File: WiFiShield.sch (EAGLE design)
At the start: 38 parts, among them IC1 74HC4050D, IC2 SPX3819M5-L-3-3, IC3 CC3000MOD, IC4 MCP9701A, J1 Test, J10 U.FL-R-SMT-1(10), J11 Mode, J12 Temp, J5 ARDUINO-SHIELD_R3, J6 101-00660-68-6

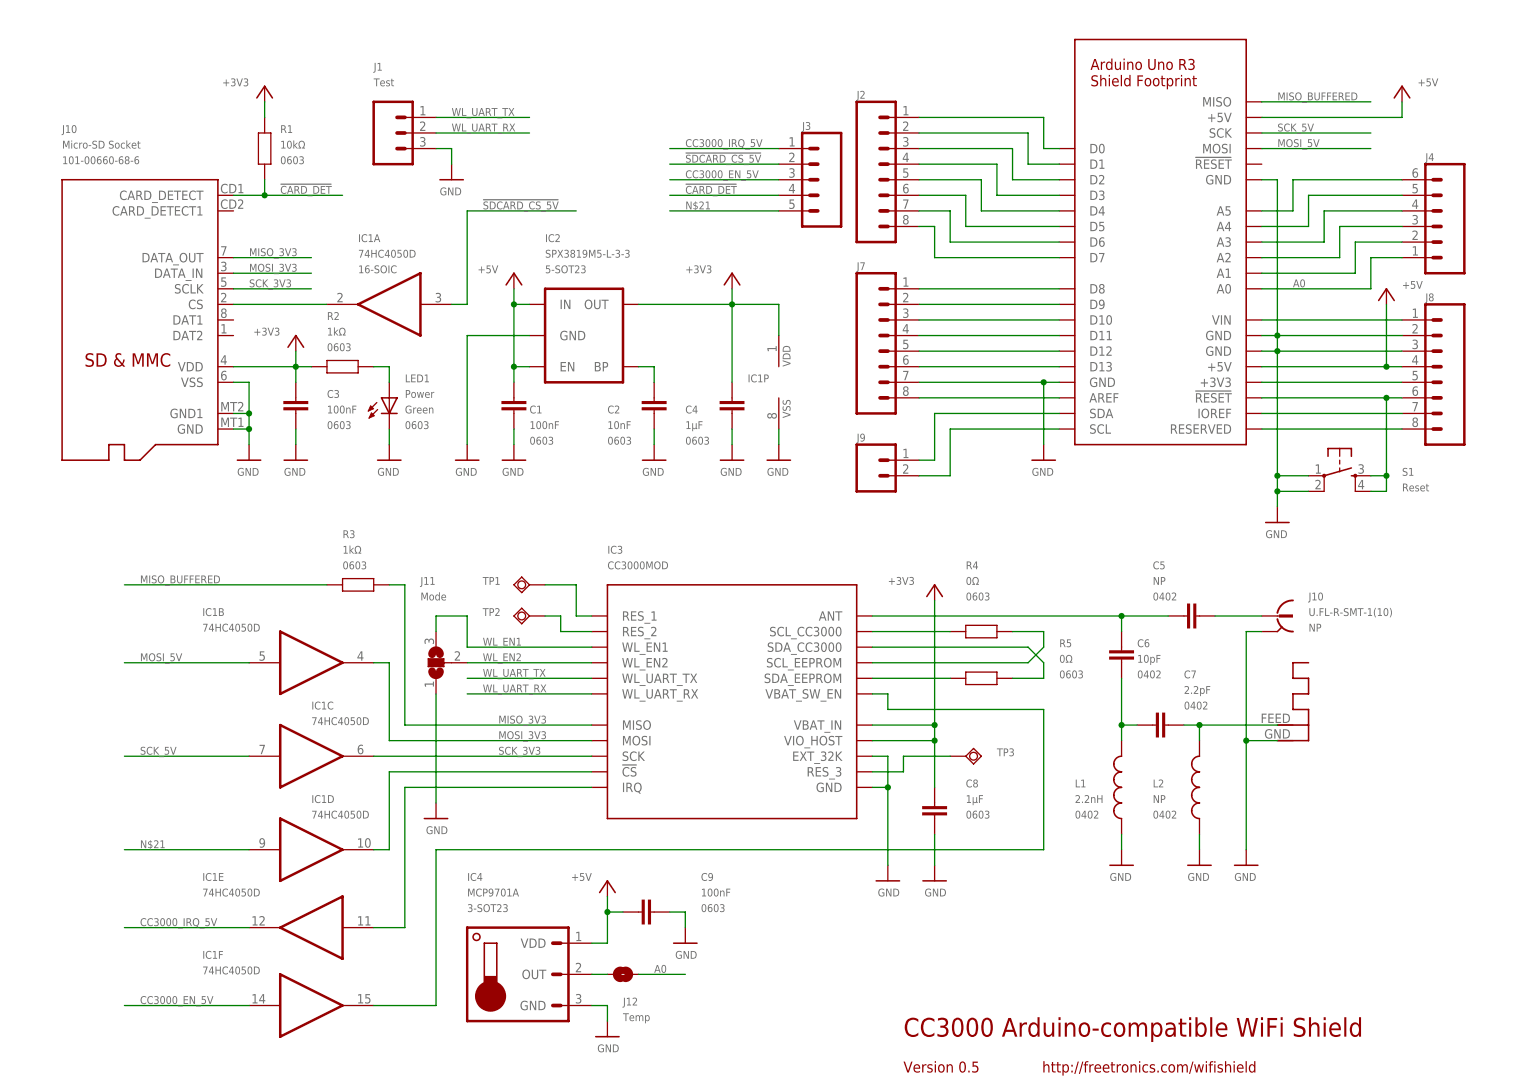
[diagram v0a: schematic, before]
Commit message: Added tristate buffer on MISO to fix CC3000 SPI bug, some minor tweaks, pull-ups added on nCS lines and CC3000 enable, silkscreen label tweaks.
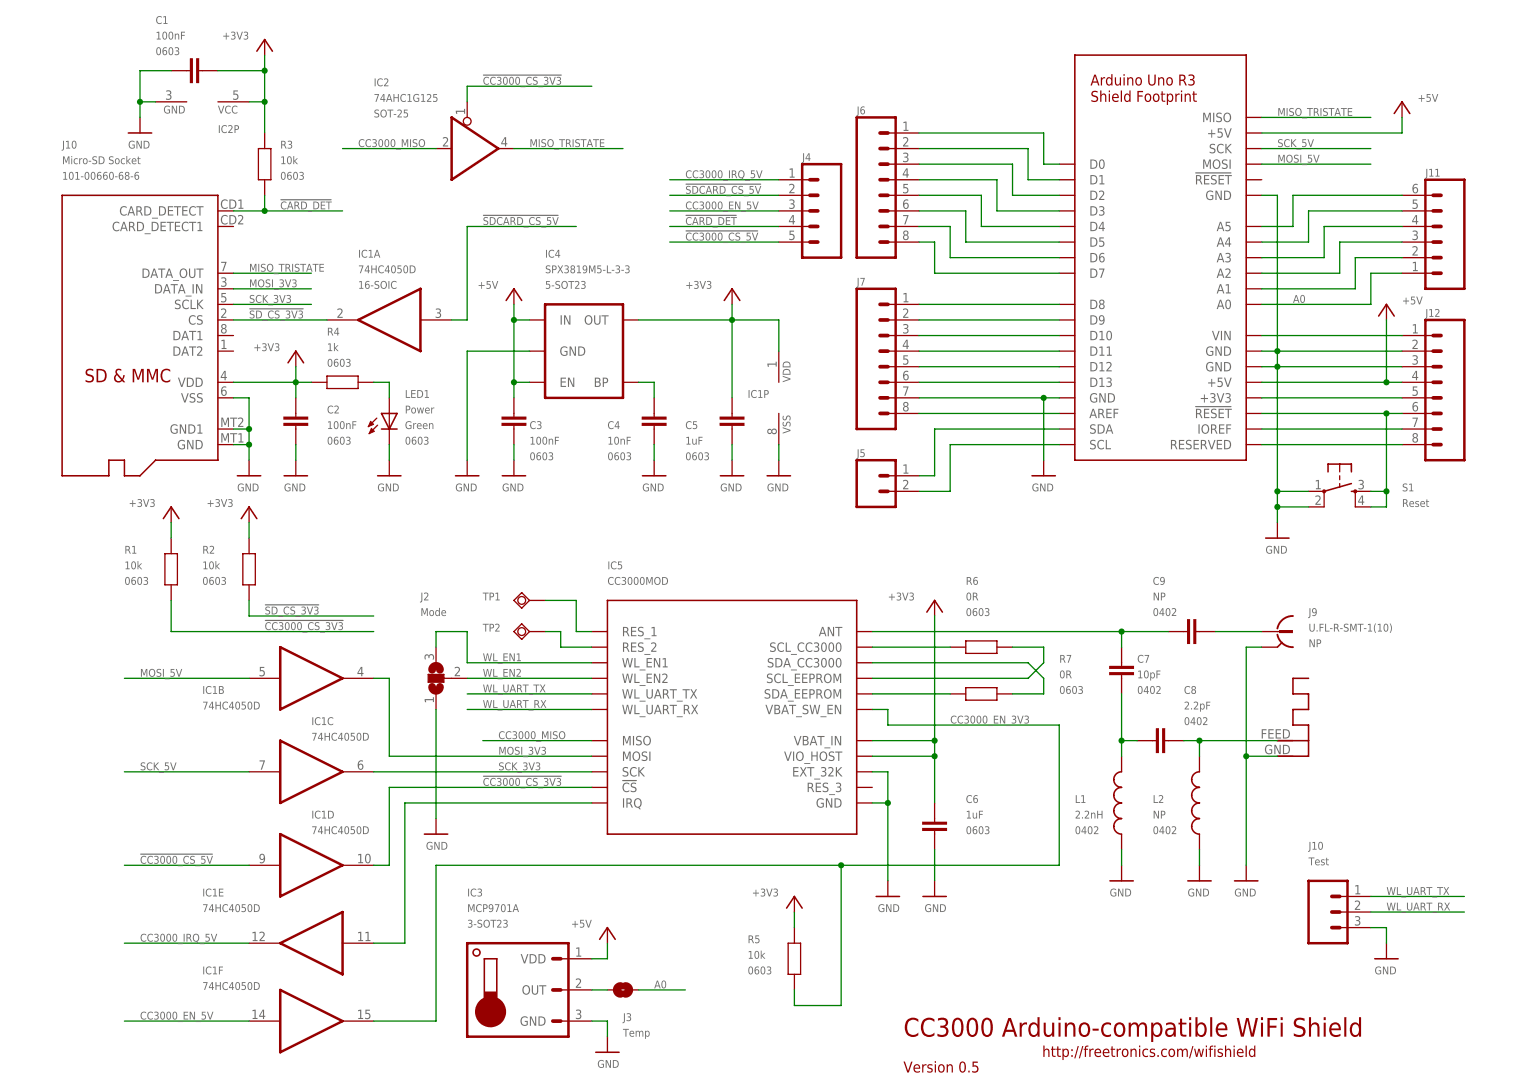
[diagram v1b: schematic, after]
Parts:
- removed TP3: R3, testpad:TPSQTP06R
- added IC5: CC3000MOD, freetronics-luke:CC3000
- added R6, R7: 0R, freetronics-master-v1:RESISTOR0603
- C2: value 10nF -> 100nF
- C4: value 1µF -> 10nF
- C5: value NP -> 1uF; device freetronics-master-v1:CAP0402 -> freetronics-master-v1:CAP0603; PACKAGE 0402 -> 0603
- C6: value 10pF -> 1uF; device freetronics-master-v1:CAP0402 -> freetronics-master-v1:CAP0603; PACKAGE 0402 -> 0603
- C7: value 2.2pF -> 10pF
- C8: value 1µF -> 2.2pF; device freetronics-master-v1:CAP0603 -> freetronics-master-v1:CAP0402; PACKAGE 0603 -> 0402
- C9: value 100nF -> NP; device freetronics-master-v1:CAP0603 -> freetronics-master-v1:CAP0402; PACKAGE 0603 -> 0402
- IC2: value SPX3819M5-L-3-3 -> 74AHC1G125; device SparkFun:V_REG_LDOSMD -> 74xx-little-de:74AHC1G125DBV; PACKAGE 5-SOT23 -> SOT-25
- IC3: value CC3000MOD -> MCP9701A; device freetronics-luke:CC3000 -> freetronics-master-v1:MCP9700SOT-23; PACKAGE (none) -> 3-SOT23
- IC4: value MCP9701A -> SPX3819M5-L-3-3; device freetronics-master-v1:MCP9700SOT-23 -> SparkFun:V_REG_LDOSMD; PACKAGE 3-SOT23 -> 5-SOT23
- J1: value Test -> 101-00660-68-6; device freetronics-master-v1:M03PTH -> RAMPSdisplay:ADAFRUIT_MICROSD; FOO (none) -> Micro-SD Socket; ID (none) -> 101-00660-68-6; NAME2 (none) -> J10
- J10: value U.FL-R-SMT-1(10) -> Test; device freetronics-luke:UFL -> freetronics-master-v1:M03PTH; NOTE NP -> (none)
- J11: value Mode -> (none); device freetronics-master-v1:SJ2W -> freetronics-master-v1:M06SIP
- J12: value Temp -> (none); device freetronics-luke:SJ -> freetronics-master-v1:M08STD
- J2: value (none) -> Mode; device freetronics-master-v1:M08STD -> freetronics-master-v1:SJ2W
- J3: value (none) -> Temp; device freetronics-master-v1:M05PTH -> freetronics-luke:SJ
- J4: device freetronics-master-v1:M06SIP -> freetronics-master-v1:M05PTH
- J5: value ARDUINO-SHIELD_R3 -> (none); device freetronics-luke:ARDUINO-SHIELD_R3 -> freetronics-master-v1:M02PTH
- J6: value 101-00660-68-6 -> (none); device RAMPSdisplay:ADAFRUIT_MICROSD -> freetronics-master-v1:M08STD; FOO Micro-SD Socket -> (none); ID 101-00660-68-6 -> (none); NAME2 J10 -> (none)
- J8: value (none) -> ARDUINO-SHIELD_R3; device freetronics-master-v1:M08STD -> freetronics-luke:ARDUINO-SHIELD_R3
- J9: value (none) -> U.FL-R-SMT-1(10); device freetronics-master-v1:M02PTH -> freetronics-luke:UFL; NOTE (none) -> NP
- R1: value 10kΩ -> 10k
- R2, R3: value 1kΩ -> 10k
- R4: value 0Ω -> 1k
- R5: value 0Ω -> 10k
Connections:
- removed net MISO_3V3: IC3.MISO, J6.DATA_OUT, R3.1
- removed net MISO_BUFFERED: J5.MISO, R3.2
- removed net N$21: IC1D.I, J3.5
- removed net N$3: IC1F.O, IC3.VBAT_SW_EN
- removed net N$35: IC1A.O, J6.CS
- removed net N$41: IC1D.O, IC3.!CS
- removed net RES_3: IC3.RES_3, TP3.TP
- new net !CC3000_CS_3V3: IC1D.O, IC2A.OE, IC5.!CS, R1.2
- new net !CC3000_CS_5V: IC1D.I, J4.5
- new net !SD_CS_3V3: IC1A.O, J1.CS, R2.2
- new net CC3000_EN_3V3: IC1F.O, IC5.VBAT_SW_EN, R5.2
- new net CC3000_MISO: IC2A.I, IC5.MISO
- new net MISO_TRISTATE: IC2A.O, J1.DATA_OUT, J8.MISO
- net !CARD_DET: now also J1.CARD_DETECT, J4.4, R3.1; no longer J3.4, J6.CARD_DETECT, R1.1
- net !SDCARD_CS_5V: now also J4.2; no longer J3.2
- net +3V3: now also C1.2, C2.1, C5.1, C6.2, IC2P.VCC, IC4.OUT, IC5.VBAT_IN, IC5.VIO_HOST, J1.VDD, R1.1, R2.1, R3.2, R4.2, R5.1; no longer C3.1, C4.1, C8.2, IC2.OUT, IC3.VBAT_IN, IC3.VIO_HOST, J6.VDD, R1.2, R2.2
- net +5V: now also C3.2, IC4.EN, IC4.IN, J12.4, J8.+5V; no longer C1.2, IC2.EN, IC2.IN, J5.+5V, J8.4
- net +5V-2: now also IC3.VDD, J8.+5V@0; no longer C9.1, IC4.VDD, J5.+5V@0
- net A0: now also J11.1, J3.2, J8.A0; no longer J12.2, J4.1, J5.A0
- net CC3000_EN_5V: now also J4.3; no longer J3.3
- net CC3000_IRQ_5V: now also J4.1; no longer J3.1
- net GND: now also C2.2, C3.1, C4.1, C5.2, C6.1, IC2P.GND, IC5.EXT_32K, IC5.GND, J1.GND, J1.GND1, J1.VSS, J10.3, J12.2, J12.3, J2.1, J8.GND, J8.GND@0, J8.GND@1, J8.GND@2, J9.GND; no longer C2.1, C3.2, C4.2, C8.1, C9.2, IC2.GND, IC3.EXT_32K, J1.3, J10.GND, J11.1, J5.GND, J5.GND@0, J5.GND@1, J5.GND@2, J6.GND, J6.GND1, J6.VSS, J8.2, J8.3
- net MOSI_3V3: now also IC5.MOSI, J1.DATA_IN; no longer IC3.MOSI, J6.DATA_IN
- net MOSI_5V: now also J8.MOSI; no longer J5.MOSI
- net N$1: now also IC5.SDA_EEPROM, R7.2; no longer IC3.SDA_EEPROM, R5.2
- net N$103: now also C7.1, C8.2; no longer C6.1, C7.2
- net N$104: now also C8.1; no longer C7.1
- net N$11: now also IC3.OUT, J3.1; no longer IC4.OUT, J12.1
- net N$123: now also J6.6, J8.D5; no longer J2.6, J5.D5
- net N$124: now also J6.7, J8.D6; no longer J2.7, J5.D6
- net N$125: now also J6.8, J8.D7; no longer J2.8, J5.D7
- net N$126: now also J5.1, J8.SDA; no longer J5.SDA, J9.1
- net N$127: now also J8.AREF; no longer J5.AREF
- net N$128: now also J8.D13; no longer J5.D13
- net N$129: now also J8.D12; no longer J5.D12
- net N$130: now also J5.2, J8.SCL; no longer J5.SCL, J9.2
- net N$131: now also J8.D8; no longer J5.D8
- net N$132: now also J8.D9; no longer J5.D9
- net N$133: now also J8.D10; no longer J5.D10
- net N$134: now also J8.D11; no longer J5.D11
- net N$15: now also IC5.SCL_CC3000, R6.2; no longer IC3.SCL_CC3000, R4.2
- net N$16: now also C7.2, C9.2, IC5.ANT; no longer C5.2, C6.2, IC3.ANT
- net N$2: now also IC5.SDA_CC3000, R7.1; no longer IC3.SDA_CC3000, R5.1
- net N$28: now also IC5.RES_2; no longer IC3.RES_2
- net N$29: now also IC5.RES_1; no longer IC3.RES_1
- net N$30: now also C9.1, J9.SIG; no longer C5.1, J10.SIG
- net N$4: now also R4.1; no longer R2.1
- net N$42: now also IC5.IRQ; no longer IC3.IRQ
- net N$43: now also C4.2, IC4.BP; no longer C2.2, IC2.BP
- net N$48: now also J11.2, J8.A1; no longer J4.2, J5.A1
- net N$49: now also J11.3, J8.A2; no longer J4.3, J5.A2
- net N$5: now also IC5.SCL_EEPROM, R6.1; no longer IC3.SCL_EEPROM, R4.1
- net N$50: now also J11.4, J8.A3; no longer J4.4, J5.A3
- net N$72: now also J11.5, J8.A4; no longer J4.5, J5.A4
- net N$73: now also J11.6, J8.A5; no longer J4.6, J5.A5
- net N$74: now also J12.8, J8.RESERVED; no longer J5.RESERVED, J8.8
- net N$75: now also J12.1, J8.VIN; no longer J5.VIN, J8.1
- net N$77: now also J12.5, J8.+3V3; no longer J5.+3V3, J8.5
- net N$78: now also J12.6, J8.!RESET; no longer J5.!RESET, J8.6
- net N$81: now also J12.7, J8.IOREF; no longer J5.IOREF, J8.7
- net N$82: now also J6.1, J8.D0; no longer J2.1, J5.D0
- net N$87: now also J6.2, J8.D1; no longer J2.2, J5.D1
- net N$88: now also J6.3, J8.D2; no longer J2.3, J5.D2
- net N$89: now also J6.4, J8.D3; no longer J2.4, J5.D3
- net N$90: now also J6.5, J8.D4; no longer J2.5, J5.D4
- net SCK_3V3: now also IC5.SCK, J1.SCLK; no longer IC3.SCK, J6.SCLK
- net SCK_5V: now also J8.SCK; no longer J5.SCK
- net WL_EN1: now also IC5.WL_EN1, J2.3; no longer IC3.WL_EN1, J11.3
- net WL_EN2: now also IC5.WL_EN2, J2.2; no longer IC3.WL_EN2, J11.2
- net WL_UART_RX: now also IC5.WL_UART_RX, J10.2; no longer IC3.WL_UART_RX, J1.2
- net WL_UART_TX: now also IC5.WL_UART_TX, J10.1; no longer IC3.WL_UART_TX, J1.1
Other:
- note removed: "PCB Stackup: 2-layer FR-4, must be 0.8 mm thick 35µm Cu both layers, with mask"
- moved on the sheet: C1, C2, C3, C4, C5, C6, C7, C8, C9, IC1A, IC1B, IC1C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

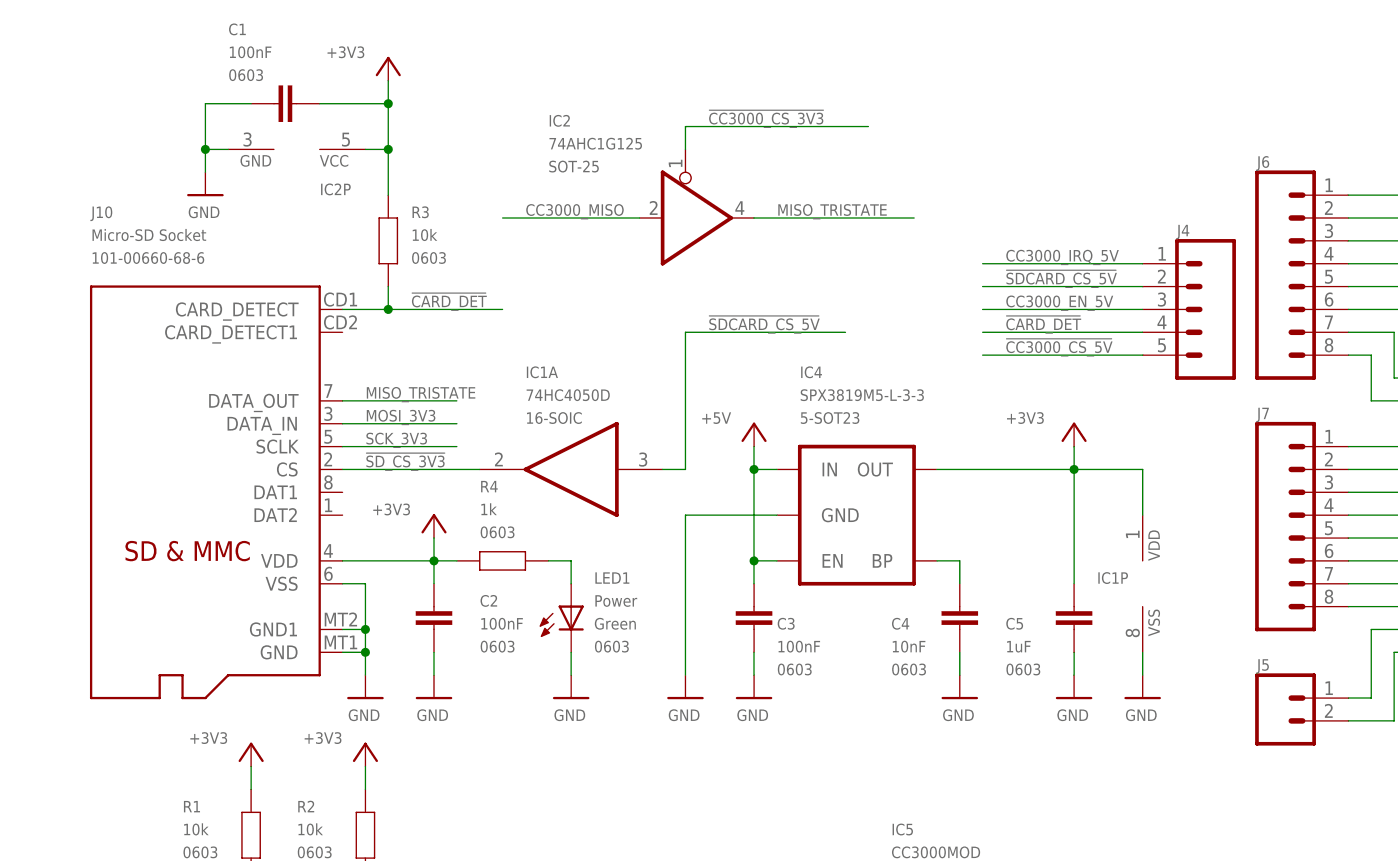
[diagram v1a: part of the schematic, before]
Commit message: Swap adafruit microsd slot for (very similar) freetronics library footprint, remove sometimes-problematic CD line
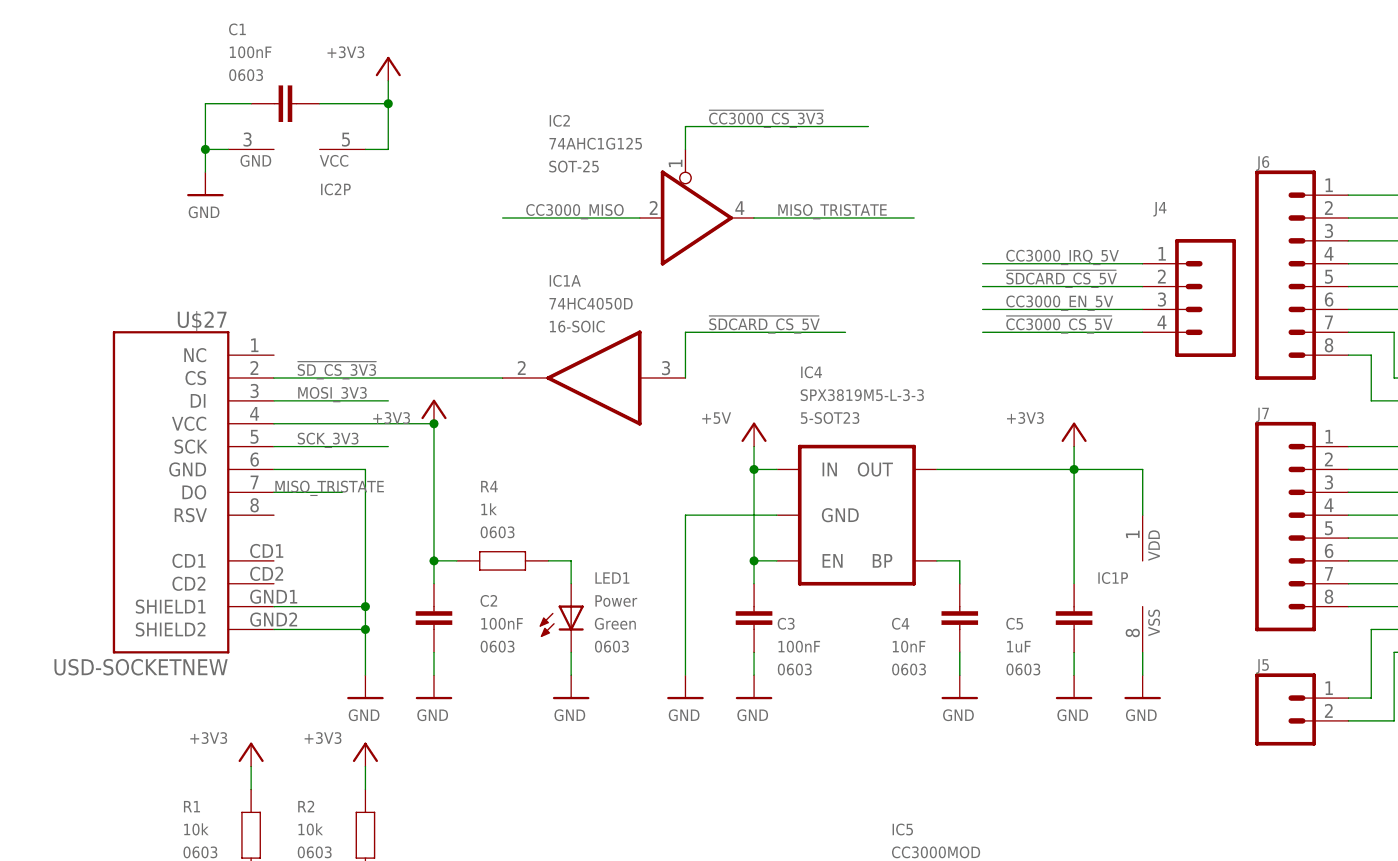
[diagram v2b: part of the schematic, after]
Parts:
- removed J1: 101-00660-68-6, RAMPSdisplay:ADAFRUIT_MICROSD
- removed R3: 10k, freetronics-master-v1:RESISTOR0603
- added U$27: USD-SOCKETNEW, freetronics-master-v1.1:USD-SOCKETNEW
- J4: device freetronics-master-v1:M05PTH -> freetronics-master-v1.1:M04PTH
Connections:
- net N$81 renamed IOREF
- removed net !CARD_DET: J1.CARD_DETECT, J4.4, R3.1
- net !CC3000_CS_5V: now also J4.4; no longer J4.5
- net !SD_CS_3V3: now also U$27.CS; no longer J1.CS
- net +3V3: now also U$27.VCC; no longer J1.VDD, R3.2
- net GND: now also U$27.GND, U$27.SHIELD1, U$27.SHIELD2; no longer J1.GND, J1.GND1, J1.VSS
- net MISO_TRISTATE: now also U$27.DO; no longer J1.DATA_OUT
- net MOSI_3V3: now also U$27.DI; no longer J1.DATA_IN
- net SCK_3V3: now also U$27.SCK; no longer J1.SCLK
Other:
- moved on the sheet: IC1A

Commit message: Swap 4050 buffer for MC74VHCT50A (stocked part, used on FTOLED.)
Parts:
- IC1: device 40xx:4050D -> freetronics-angus:MC74VHCT50A
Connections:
- net +3V3: now also IC1P.VCC; no longer IC1P.VDD
- net CC3000_EN_3V3: now also IC1E.O; no longer IC1F.O
- net CC3000_EN_5V: now also IC1E.I; no longer IC1F.I
- net CC3000_IRQ_5V: now also IC1F.O; no longer IC1E.O
- net GND: now also IC1P.GND; no longer IC1P.VSS
- net N$42: now also IC1F.I; no longer IC1E.I
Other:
- note added: "SPI lines connected to 6-pin ISP header for R3 compatibility."
- note removed: "SPI lines connected to 6-pin ISP header for Leonardo compatibility."
- moved on the sheet: IC1E, IC1F
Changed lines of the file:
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@@
 <part name="ANT1" library="adafruit" deviceset="ANTENNA" device=""/>
 <part name="U$2" library="freetronics-luke" deviceset="GND" device=""/>
-<part name="IC1" library="40xx" deviceset="4050" device="D" value="74HC4050D">
+<part name="IC1" library="freetronics-angus" deviceset="MC74VHCT50A" device="" value="74HC4050D">
 <attribute name="PACKAGE" value="16-SOIC"/>
 </part>
@@
 antenna; 50Ω 2.4 GHz</text>
 <text x="205.74" y="167.64" size="1.27" layer="98">SPI lines connected to 6-pin ISP
-header for Leonardo compatibility.</text>
+header for R3 compatibility.</text>
 <wire x1="134.62" y1="152.4" x2="142.24" y2="152.4" width="0.1524" layer="98" style="dashdot"/>
 <wire x1="142.24" y1="127" x2="139.7" y2="127" width="0.1524" layer="98" style="dashdot"/>
@@
 <instance part="ANT1" gate="G$1" x="208.28" y="60.96" rot="R270"/>
 <instance part="U$2" gate="G$1" x="40.64" y="104.14" rot="MR0"/>
-<instance part="IC1" gate="E" x="50.8" y="27.94" smashed="yes" rot="R180">
+<instance part="IC1" gate="F" x="50.8" y="27.94" smashed="yes" rot="R180">
 <attribute name="NAME" x="33.02" y="35.56" size="1.27" layer="95"/>
 <attribute name="VALUE" x="33.02" y="33.02" size="1.27" layer="96"/>
@@
 <attribute name="NAME" x="128.27" y="157.988" size="1.27" layer="95"/>
 </instance>
-<instance part="IC1" gate="F" x="50.8" y="15.24" smashed="yes">
+<instance part="IC1" gate="E" x="50.8" y="15.24" smashed="yes">
 <attribute name="NAME" x="33.02" y="22.86" size="1.27" layer="95"/>
 <attribute name="VALUE" x="33.02" y="20.32" size="1.27" layer="96"/>
@@
 </segment>
 <segment>
-<pinref part="IC1" gate="P" pin="VSS"/>
+<pinref part="IC1" gate="P" pin="GND"/>
 <pinref part="U$3" gate="G$1" pin="GND"/>
 <wire x1="127" y1="106.68" x2="127" y2="109.22" width="0.1524" layer="91"/>
@@
 <pinref part="U$15" gate="G$1" pin="+3V3"/>
 <wire x1="119.38" y1="132.08" x2="119.38" y2="129.54" width="0.1524" layer="91"/>
-<pinref part="IC1" gate="P" pin="VDD"/>
+<pinref part="IC1" gate="P" pin="VCC"/>
 <wire x1="119.38" y1="129.54" x2="127" y2="129.54" width="0.1524" layer="91"/>
 <wire x1="127" y1="129.54" x2="127" y2="124.46" width="0.1524" layer="91"/>
@@
 <net name="CC3000_IRQ_5V" class="0">
 <segment>
-<pinref part="IC1" gate="E" pin="O"/>
+<pinref part="IC1" gate="F" pin="O"/>
 <wire x1="40.64" y1="27.94" x2="20.32" y2="27.94" width="0.1524" layer="91"/>
 <label x="22.86" y="28.194" size="1.27" layer="95"/>
@@
 <wire x1="96.52" y1="50.8" x2="66.04" y2="50.8" width="0.1524" layer="91"/>
 <wire x1="66.04" y1="50.8" x2="66.04" y2="27.94" width="0.1524" layer="91"/>
-<pinref part="IC1" gate="E" pin="I"/>
+<pinref part="IC1" gate="F" pin="I"/>
 <wire x1="66.04" y1="27.94" x2="60.96" y2="27.94" width="0.1524" layer="91"/>
 </segment>
@@
 </segment>
 <segment>
-<pinref part="IC1" gate="F" pin="I"/>
+<pinref part="IC1" gate="E" pin="I"/>
 <wire x1="40.64" y1="15.24" x2="20.32" y2="15.24" width="0.1524" layer="91"/>
 <label x="22.86" y="15.494" size="1.27" layer="95"/>
@@
 <net name="CC3000_EN_3V3" class="0">
 <segment>
-<pinref part="IC1" gate="F" pin="O"/>
+<pinref part="IC1" gate="E" pin="O"/>
 <wire x1="60.96" y1="15.24" x2="71.12" y2="15.24" width="0.1524" layer="91"/>
 <wire x1="71.12" y1="15.24" x2="71.12" y2="40.64" width="0.1524" layer="91"/>
